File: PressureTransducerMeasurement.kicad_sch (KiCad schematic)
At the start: 12 parts, among them J12 PT_1, J13 PT_4, J14 PT_2, J15 PT_5, J16 PT_3, J17 PT_6

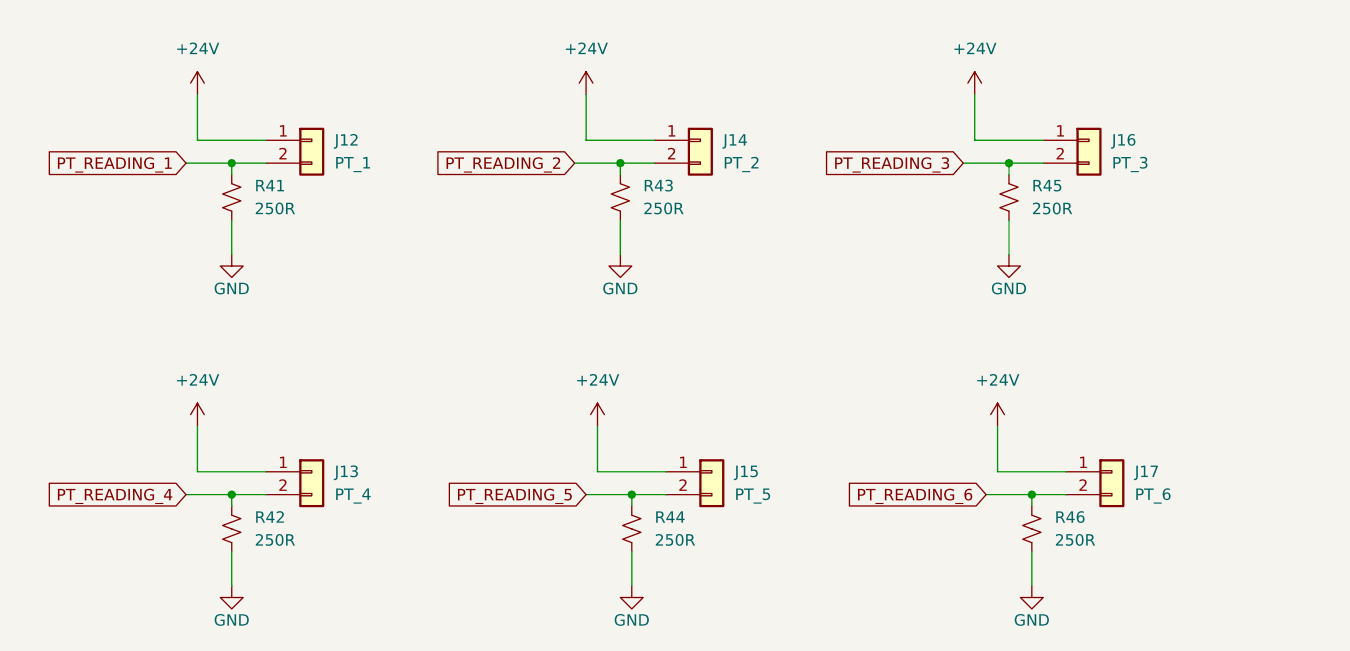
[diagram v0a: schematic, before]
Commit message: revamped schematic to be more readable
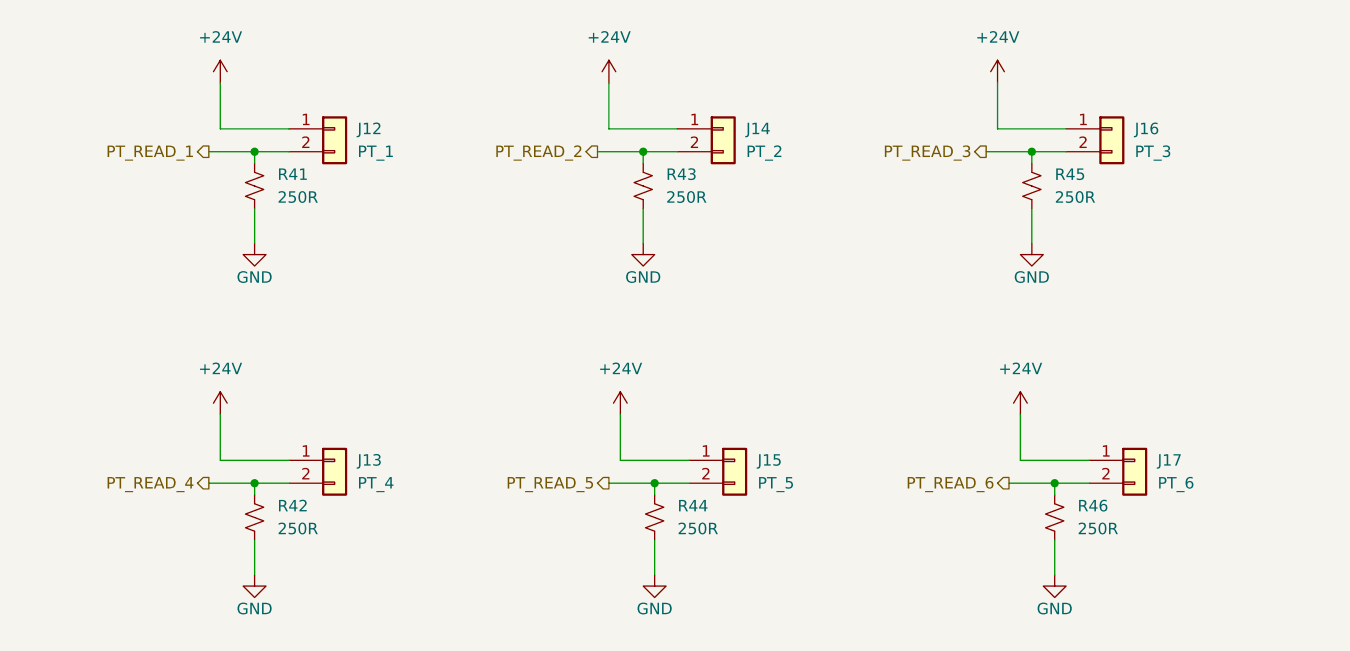
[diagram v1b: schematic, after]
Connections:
- net PT_READING_1 renamed PT_READ_1
- net PT_READING_2 renamed PT_READ_2
- net PT_READING_3 renamed PT_READ_3
- net PT_READING_4 renamed PT_READ_4
- net PT_READING_5 renamed PT_READ_5
- net PT_READING_6 renamed PT_READ_6
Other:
- moved on the sheet: J12, J13, J14, J15, J16, J17, R41, R42, R43, R44, R45, R46

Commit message: add power sequencing
add usb VBUS ORing
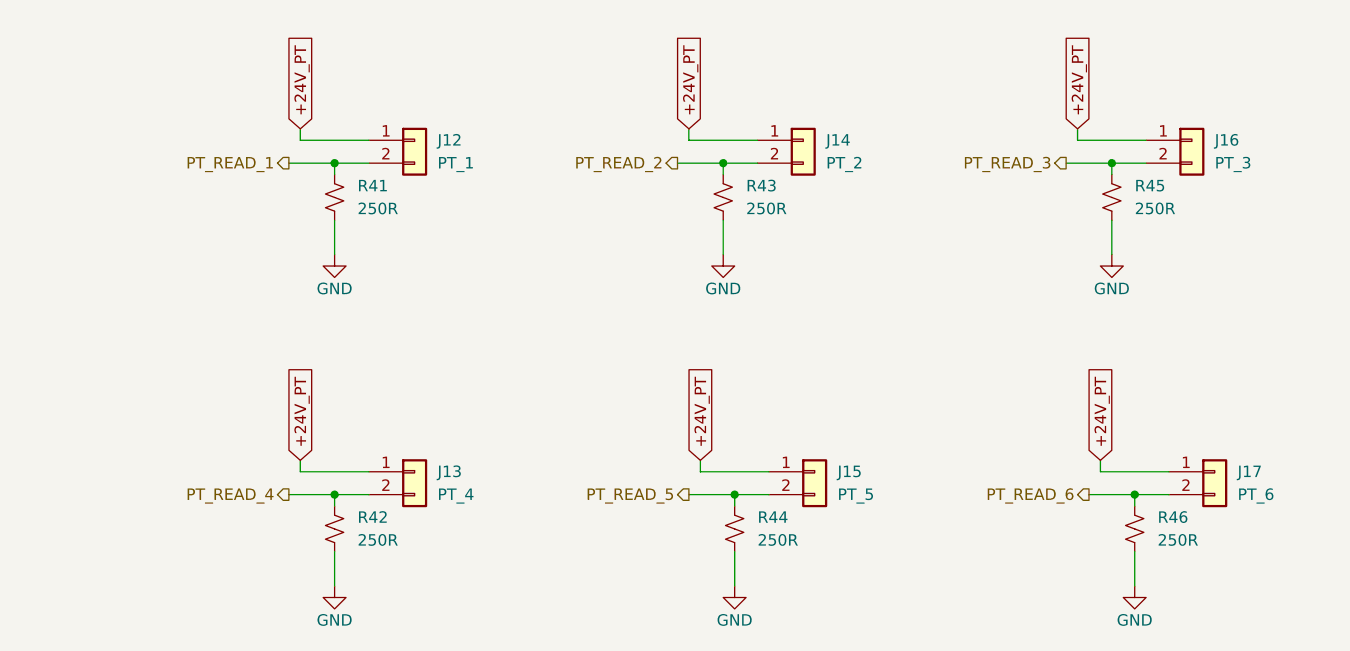
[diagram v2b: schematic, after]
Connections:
- net +24V renamed +24V_PT
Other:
- moved on the sheet: J12, J13, J14, J15, J16, J17, R41, R42, R43, R44, R45, R46

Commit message: add 2 stage lockout to ignitor, add ignitor resistance reading with adc current source
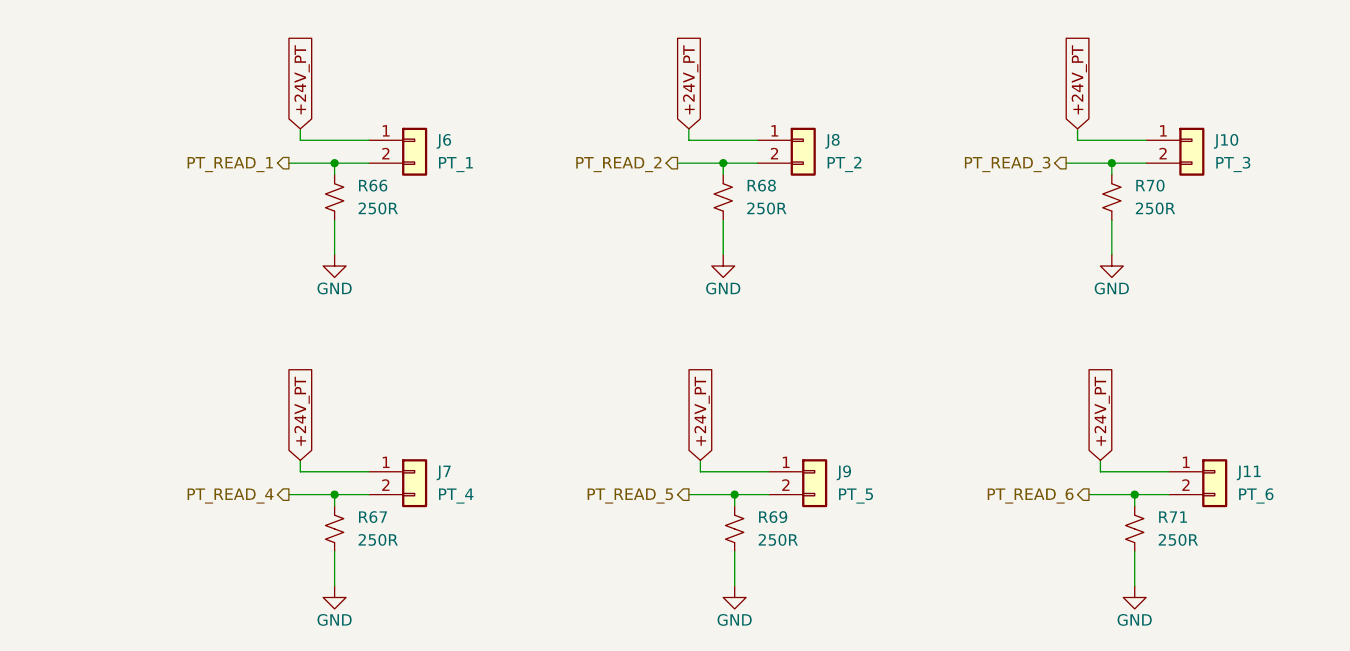
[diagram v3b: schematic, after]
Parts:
- renumbered J16 to J10, J17 to J11, J12 to J6, J13 to J7, J14 to J8, J15 to J9, R41 to R66, R42 to R67, R43 to R68, R44 to R69, R45 to R70, R46 to R71
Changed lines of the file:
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@@
 		(dnp no)
 		(fields_autoplaced yes)
-		(property "Reference" "J16"
+		(property "Reference" "J10"
 			(at 208.28 74.9299 0)
 			(effects
@@
 			(project "nexus"
 				(path "/226c5870-4123-4efa-a2b3-b42d02f59bb7/51db055d-2275-4f1e-94b0-c8fb03c9970a"
-					(reference "J16")
+					(reference "J10")
 					(unit 1)
 				)
@@
 		(dnp no)
 		(fields_autoplaced yes)
-		(property "Reference" "J17"
+		(property "Reference" "J11"
 			(at 210.82 111.7599 0)
 			(effects
@@
 			(project "nexus"
 				(path "/226c5870-4123-4efa-a2b3-b42d02f59bb7/51db055d-2275-4f1e-94b0-c8fb03c9970a"
-					(reference "J17")
+					(reference "J11")
 					(unit 1)
 				)
@@
 		(on_board yes)
 		(dnp no)
-		(property "Reference" "#PWR0102"
+		(property "Reference" "#PWR0152"
 			(at 110.49 130.81 0)
 			(effects
@@
 			(project "nexus"
 				(path "/226c5870-4123-4efa-a2b3-b42d02f59bb7/51db055d-2275-4f1e-94b0-c8fb03c9970a"
-					(reference "#PWR0102")
+					(reference "#PWR0152")
 					(unit 1)
 				)
@@
 		(dnp no)
 		(fields_autoplaced yes)
-		(property "Reference" "R46"
+		(property "Reference" "R71"
 			(at 201.93 116.8399 0)
 			(effects
@@
 			(project "nexus"
 				(path "/226c5870-4123-4efa-a2b3-b42d02f59bb7/51db055d-2275-4f1e-94b0-c8fb03c9970a"
-					(reference "R46")
+					(reference "R71")
 					(unit 1)
 				)
@@
 		(dnp no)
 		(fields_autoplaced yes)
-		(property "Reference" "R41"
+		(property "Reference" "R66"
 			(at 113.03 80.0099 0)
 			(effects
@@
 			(project ""
 				(path "/226c5870-4123-4efa-a2b3-b42d02f59bb7/51db055d-2275-4f1e-94b0-c8fb03c9970a"
-					(reference "R41")
+					(reference "R66")
 					(unit 1)
 				)
@@
 		(on_board yes)
 		(dnp no)
-		(property "Reference" "#PWR0101"
+		(property "Reference" "#PWR0151"
 			(at 110.49 93.98 0)
 			(effects
@@
 			(project "nexus"
 				(path "/226c5870-4123-4efa-a2b3-b42d02f59bb7/51db055d-2275-4f1e-94b0-c8fb03c9970a"
-					(reference "#PWR0101")
+					(reference "#PWR0151")
 					(unit 1)
 				)
@@
 		(dnp no)
 		(fields_autoplaced yes)
-		(property "Reference" "R44"
+		(property "Reference" "R69"
 			(at 157.48 116.8399 0)
 			(effects
@@
 			(project "nexus"
 				(path "/226c5870-4123-4efa-a2b3-b42d02f59bb7/51db055d-2275-4f1e-94b0-c8fb03c9970a"
-					(reference "R44")
+					(reference "R69")
 					(unit 1)
 				)
@@
 		(on_board yes)
 		(dnp no)
-		(property "Reference" "#PWR0110"
+		(property "Reference" "#PWR0156"
 			(at 199.39 130.81 0)
 			(effects
@@
 			(project "nexus"
 				(path "/226c5870-4123-4efa-a2b3-b42d02f59bb7/51db055d-2275-4f1e-94b0-c8fb03c9970a"
-					(reference "#PWR0110")
+					(reference "#PWR0156")
 					(unit 1)
 				)
@@
 		(on_board yes)
 		(dnp no)
-		(property "Reference" "#PWR0106"
+		(property "Reference" "#PWR0154"
 			(at 154.94 130.81 0)
 			(effects
@@
 			(project "nexus"
 				(path "/226c5870-4123-4efa-a2b3-b42d02f59bb7/51db055d-2275-4f1e-94b0-c8fb03c9970a"
-					(reference "#PWR0106")
+					(reference "#PWR0154")
 					(unit 1)
 				)
@@
 		(dnp no)
 		(fields_autoplaced yes)
-		(property "Reference" "R45"
+		(property "Reference" "R70"
 			(at 199.39 80.0099 0)
 			(effects
@@
 			(project "nexus"
 				(path "/226c5870-4123-4efa-a2b3-b42d02f59bb7/51db055d-2275-4f1e-94b0-c8fb03c9970a"
-					(reference "R45")
+					(reference "R70")
 					(unit 1)
 				)
@@
 		(dnp no)
 		(fields_autoplaced yes)
-		(property "Reference" "J13"
+		(property "Reference" "J7"
 			(at 121.92 111.7599 0)
 			(effects
@@
 			(project "nexus"
 				(path "/226c5870-4123-4efa-a2b3-b42d02f59bb7/51db055d-2275-4f1e-94b0-c8fb03c9970a"
-					(reference "J13")
+					(reference "J7")
 					(unit 1)
 				)
@@
 		(dnp no)
 		(fields_autoplaced yes)
-		(property "Reference" "J14"
+		(property "Reference" "J8"
 			(at 165.1 74.9299 0)
 			(effects
@@
 			(project "nexus"
 				(path "/226c5870-4123-4efa-a2b3-b42d02f59bb7/51db055d-2275-4f1e-94b0-c8fb03c9970a"
-					(reference "J14")
+					(reference "J8")
 					(unit 1)
 				)
@@
 		(on_board yes)
 		(dnp no)
-		(property "Reference" "#PWR0105"
+		(property "Reference" "#PWR0153"
 			(at 153.67 93.98 0)
 			(effects
@@
 			(project "nexus"
 				(path "/226c5870-4123-4efa-a2b3-b42d02f59bb7/51db055d-2275-4f1e-94b0-c8fb03c9970a"
-					(reference "#PWR0105")
+					(reference "#PWR0153")
 					(unit 1)
 				)
@@
 		(dnp no)
 		(fields_autoplaced yes)
-		(property "Reference" "J15"
+		(property "Reference" "J9"
 			(at 166.37 111.7599 0)
 			(effects
@@
 			(project "nexus"
 				(path "/226c5870-4123-4efa-a2b3-b42d02f59bb7/51db055d-2275-4f1e-94b0-c8fb03c9970a"
-					(reference "J15")
+					(reference "J9")
 					(unit 1)
 				)
@@
 		(dnp no)
 		(fields_autoplaced yes)
-		(property "Reference" "J12"
+		(property "Reference" "J6"
 			(at 121.92 74.9299 0)
 			(effects
@@
 			(project "nexus"
 				(path "/226c5870-4123-4efa-a2b3-b42d02f59bb7/51db055d-2275-4f1e-94b0-c8fb03c9970a"
-					(reference "J12")
+					(reference "J6")
 					(unit 1)
 				)
@@
 		(dnp no)
 		(fields_autoplaced yes)
-		(property "Reference" "R42"
+		(property "Reference" "R67"
 			(at 113.03 116.8399 0)
 			(effects
@@
 			(project "nexus"
 				(path "/226c5870-4123-4efa-a2b3-b42d02f59bb7/51db055d-2275-4f1e-94b0-c8fb03c9970a"
-					(reference "R42")
+					(reference "R67")
 					(unit 1)
 				)
@@
 		(on_board yes)
 		(dnp no)
-		(property "Reference" "#PWR0109"
+		(property "Reference" "#PWR0155"
 			(at 196.85 93.98 0)
 			(effects
@@
 			(project "nexus"
 				(path "/226c5870-4123-4efa-a2b3-b42d02f59bb7/51db055d-2275-4f1e-94b0-c8fb03c9970a"
-					(reference "#PWR0109")
+					(reference "#PWR0155")
 					(unit 1)
 				)
@@
 		(dnp no)
 		(fields_autoplaced yes)
-		(property "Reference" "R43"
+		(property "Reference" "R68"
 			(at 156.21 80.0099 0)
 			(effects
@@
 			(project "nexus"
 				(path "/226c5870-4123-4efa-a2b3-b42d02f59bb7/51db055d-2275-4f1e-94b0-c8fb03c9970a"
-					(reference "R43")
-					(unit 1)
-				)
+					(reference "R68")
+					(unit 1)
+				)

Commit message: add rc filters to pressure transducer power in to filter 500khz signal on 24v rail
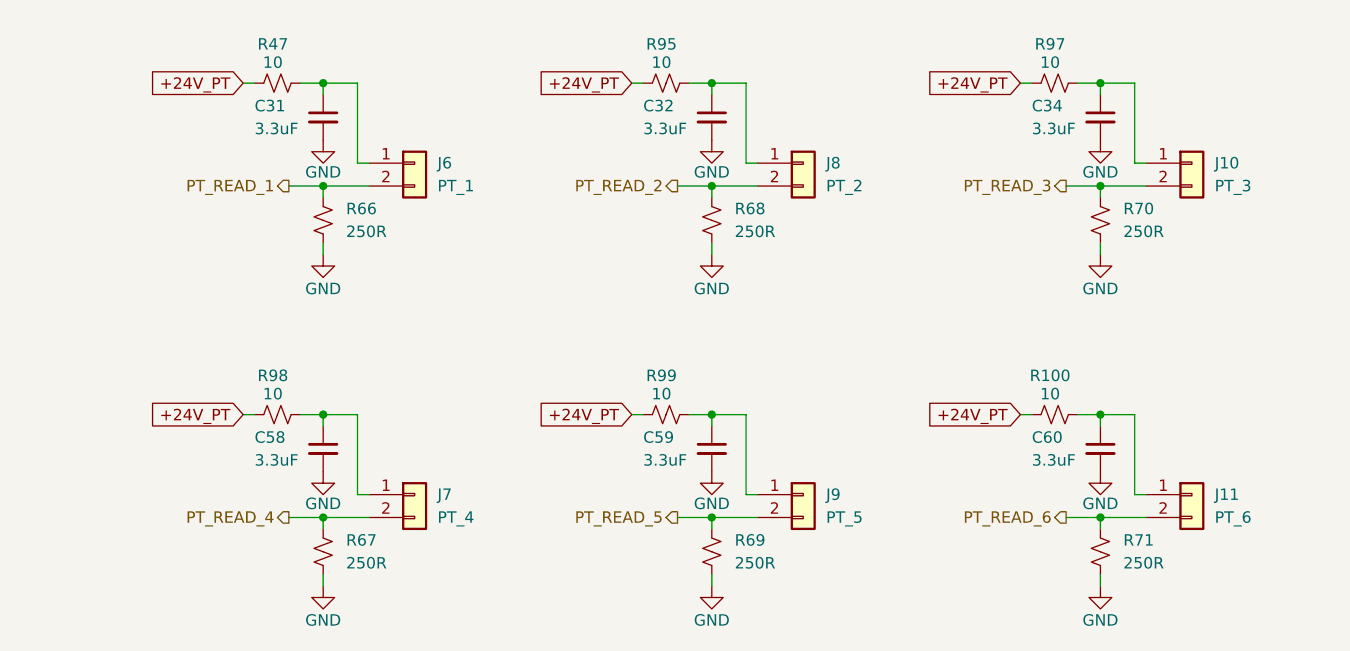
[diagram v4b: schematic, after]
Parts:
- added C31, C32, C34, C58, C59, C60: 3.3uF, symbol Device:C_Small
- added R100, R47, R95, R97, R98, R99: 10, symbol Device:R_Small_US
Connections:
- net +24V_PT: now also R100.1, R47.1, R95.1, R97.1, R98.1, R99.1; no longer J10.1 (Pin_1), J11.1 (Pin_1), J6.1 (Pin_1), J7.1 (Pin_1), J8.1 (Pin_1), J9.1 (Pin_1)
- net GND: now also C31.2, C32.2, C34.2, C58.2, C59.2, C60.2
- new net: C34.1, J10.1 (Pin_1), R97.2
- new net: C60.1, J11.1 (Pin_1), R100.2
- new net: C32.1, J8.1 (Pin_1), R95.2
- new net: C58.1, J7.1 (Pin_1), R98.2
- new net: C59.1, J9.1 (Pin_1), R99.2
- new net: C31.1, J6.1 (Pin_1), R47.2
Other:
- moved on the sheet: J10, J11, J6, J7, J8, J9, R66, R67, R68, R69, R70, R71

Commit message: add capacitor and resistor footprints
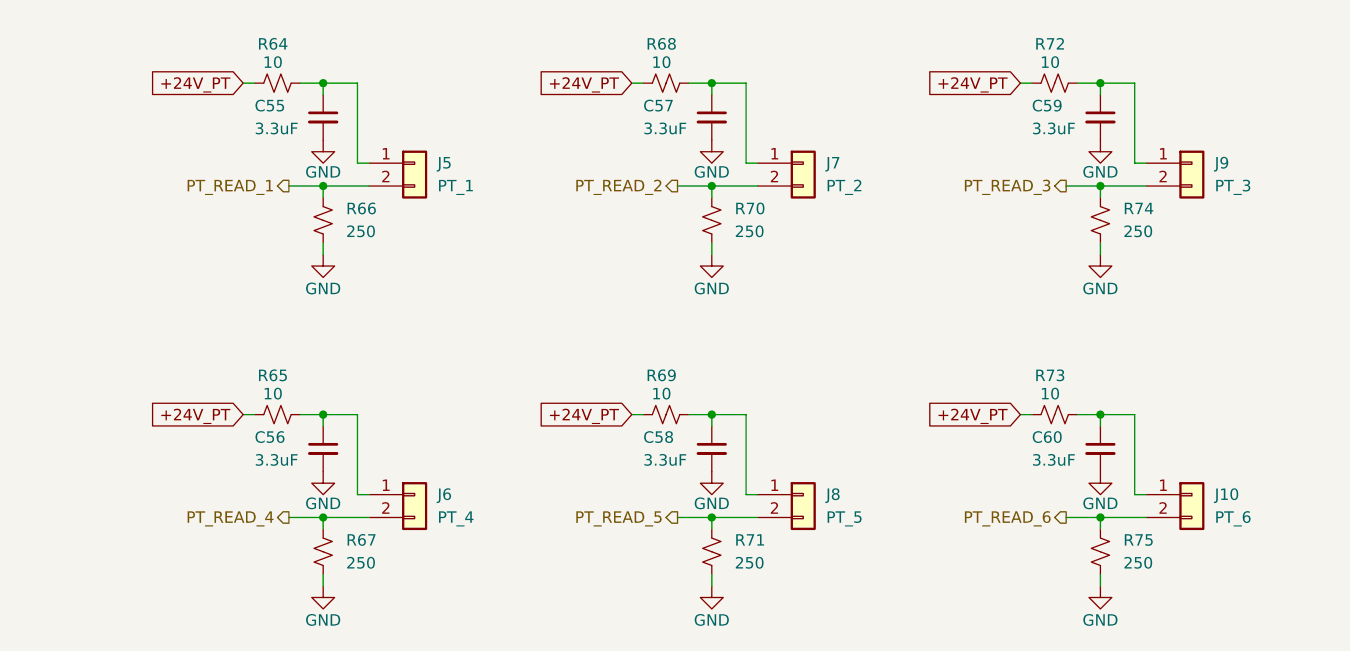
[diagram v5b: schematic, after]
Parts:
- removed C32, C34: 3.3uF, symbol Device:C_Small
- removed R100, R95, R97, R98, R99: 10, symbol Device:R_Small_US
- added C56, C57: 3.3uF, Capacitor_SMD:C_0805_2012Metric, symbol Device:C_Small
- added R65, R68, R69, R72, R73: 10, Resistor_SMD:R_0402_1005Metric, symbol Device:R_Small_US
- C55: renamed from C31; footprint (none) -> Capacitor_SMD:C_0805_2012Metric; LCSC (none) -> C342775
- C58, C59, C60: footprint (none) -> Capacitor_SMD:C_0805_2012Metric; LCSC (none) -> C342775
- R64: renamed from R47; footprint (none) -> Resistor_SMD:R_0402_1005Metric
- R66, R67: value 250R -> 250
- R70: renamed from R68; value 250R -> 250
- R71: renamed from R69; value 250R -> 250
- R74: renamed from R70; value 250R -> 250
- R75: renamed from R71; value 250R -> 250
- renumbered J11 to J10, J6 to J5, J7 to J6, J8 to J7, J9 to J8, J10 to J9
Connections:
- net +24V_PT: now also R65.1, R68.1, R69.1, R72.1, R73.1
- net GND: now also C56.2, C57.2
- net at J9.1 (Pin_1): now also C59.1, R72.2
- net at C60.1, J10.1 (Pin_1): now also R73.2
- net at J7.1 (Pin_1): now also C57.1, R68.2
- net at J6.1 (Pin_1): now also C56.1, R65.2; no longer C58.1
- net at J8.1 (Pin_1): now also C58.1, R69.2; no longer C59.1
